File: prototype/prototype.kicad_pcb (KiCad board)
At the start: 4 copper layers, 78.7 x 63.5 mm, 47 parts, among them P1 CONN_25X2, P2 CONN_25X2, P3 VGACONN, U1 MC68SEC000, U2 FLASHROM_512K_16, U3 RAM_512K_16, U4 RAM_512K_16

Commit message: Reassign mojo header pins to move VGA to the other end.
There is no room at the left-hand edge for the VGA connector because the
AVR header is in the way, so we need to move it to the right-hand edge.
To ease routing, the signals should therefore be exposed at that end too.
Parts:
- moved D10 360.0 mm to (55.5, 48.9)
- moved D5 360.0 mm to (39.0, 48.9)
- moved D6 360.0 mm to (45.5, 48.9)
- moved D7 360.0 mm to (52.0, 48.9)
- moved D8 360.0 mm to (42.5, 48.9)
- moved D9 360.0 mm to (49.0, 48.9)
- moved P3 360.0 mm to (48.0, 34.9)
- moved R11 360.0 mm to (58.6, 57.0)
- moved R13 360.0 mm to (54.8, 57.0)
- moved R14 360.0 mm to (69.4, 40.5)
- moved R15 360.0 mm to (69.4, 42.4)
- moved R2 360.0 mm to (38.9, 57.0)
- moved R4 360.0 mm to (42.7, 57.0)
- moved R7 360.0 mm to (49.7, 57.0)
- moved R9 360.0 mm to (45.9, 57.0)
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
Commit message: Assign appropriate footprints to the memory ICs.
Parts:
- D1, D10, D2, D3, D4, D5, D6, D7, D8, D9: footprint Diodes_SMD:Diode_SOT23_Handsoldering -> 68k-computer:SOT-23_Diode
- U2: footprint SSOP_Packages:TSSOP-48_6.1x12.5mm_Pitch0.5mm -> 68k-computer:TSOP-48
- U3, U4: footprint SMD_Packages:PLCC-44 -> 68k-computer:TSOP-44
- moved U2 324.6 mm to (134.6, 101.6), turned to 270 degrees
- moved U4 252.1 mm to (158.1, 80.0), turned to 90 degrees
- moved D1 218.5 mm to (229.7, 41.3)
- moved D2 218.5 mm to (229.2, 25.3)
- moved D3 218.5 mm to (239.2, 33.3)
- moved D4 218.5 mm to (228.7, 33.8)
- moved U3 200.5 mm to (134.6, 80.0), turned to 90 degrees
- moved P3 187.9 mm to (188.5, 159.7), turned to 0 degrees
- moved D5 185.7 mm to (197.5, 145.7), turned to 180 degrees
- moved R3 181.5 mm to (199.6, 137.6), turned to 90 degrees
- moved D8 179.7 mm to (194.0, 145.7), turned to 180 degrees
- moved R2 178.0 mm to (197.7, 137.6), turned to 90 degrees
- moved D6 174.7 mm to (191.0, 145.7), turned to 180 degrees
- moved R5 174.7 mm to (195.8, 137.6), turned to 90 degrees
- moved R4 171.3 mm to (193.8, 137.6), turned to 90 degrees
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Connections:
- P1 pad 10: RED3 -> A1
- P1 pad 11: GREEN0 -> A2
- P1 pad 12: GREEN1 -> A3
- P1 pad 13: GREEN2 -> A4
- P1 pad 14: GREEN3 -> A5
- P1 pad 15: ~BERR -> A6
- P1 pad 16: ~IPL2 -> A7
- P1 pad 17: ~IPL1 -> A8
- P1 pad 18: ~IPL0 -> A9
- P1 pad 19: FC2 -> A10
- P1 pad 20: FC1 -> A11
- P1 pad 21: FC0 -> LA12
- P1 pad 22: A1 -> LA13
- P1 pad 23: A2 -> LA14
- P1 pad 24: A3 -> LA15
- P1 pad 25: A4 -> LA16
- P1 pad 26: A5 -> LA17
- P1 pad 27: A6 -> LA18
- P1 pad 28: A7 -> LA19
- P1 pad 29: A8 -> LA20
- P1 pad 30: A9 -> LA21
- P1 pad 31: A10 -> LA22
- P1 pad 32: A11 -> LA23
- P1 pad 33: LA12 -> RED0
- P1 pad 34: LA13 -> RED1
- P1 pad 35: LA14 -> RED2
- P1 pad 36: LA15 -> RED3
- P1 pad 37: LA16 -> GREEN0
- P1 pad 38: LA17 -> GREEN1
- P1 pad 39: LA18 -> GREEN2
- P1 pad 40: LA19 -> GREEN3
- P1 pad 41: LA20 -> BLUE0
- P1 pad 42: LA21 -> BLUE1
- P1 pad 43: LA22 -> BLUE2
- P1 pad 44: LA23 -> BLUE3
- P1 pad 7: RED0 -> FC2
- P1 pad 8: RED1 -> FC1
- P1 pad 9: RED2 -> FC0
- P2 pad 10: BLUE3 -> PA17
- P2 pad 11: PA12 -> PA18
- P2 pad 12: PA13 -> PA19
- P2 pad 13: PA14 -> ~RE
- P2 pad 14: PA15 -> ~WE
- P2 pad 15: PA16 -> ~IPL0
- P2 pad 16: PA17 -> ~IPL1
- P2 pad 17: PA18 -> ~IPL2
- P2 pad 18: PA19 -> ~BERR
- P2 pad 19: ~RE -> CLK
- P2 pad 20: ~WE -> ~DTACK
- P2 pad 21: CLK -> R/~W
- P2 pad 22: ~DTACK -> ~LDS
- P2 pad 23: R/~W -> ~UDS
- P2 pad 24: ~LDS -> ~AS
- P2 pad 25: ~UDS -> D0
- P2 pad 26: ~AS -> D1
- P2 pad 27: D0 -> D2
- P2 pad 28: D1 -> D3
- P2 pad 29: D2 -> D4
- P2 pad 30: D3 -> D5
- P2 pad 31: D4 -> D6
- P2 pad 32: D5 -> D7
- P2 pad 33: D6 -> D8
- P2 pad 34: D7 -> D9
- P2 pad 35: D8 -> D10
- P2 pad 36: D9 -> D11
- P2 pad 37: D10 -> D12
- P2 pad 38: D11 -> D13
- P2 pad 39: D12 -> D14
- P2 pad 40: D13 -> D15
- P2 pad 41: D14 -> HSYNC
- P2 pad 42: D15 -> VSYNC
- P2 pad 5: HSYNC -> PA12
- P2 pad 6: VSYNC -> PA13
- P2 pad 7: BLUE0 -> PA14
- P2 pad 8: BLUE1 -> PA15
- P2 pad 9: BLUE2 -> PA16

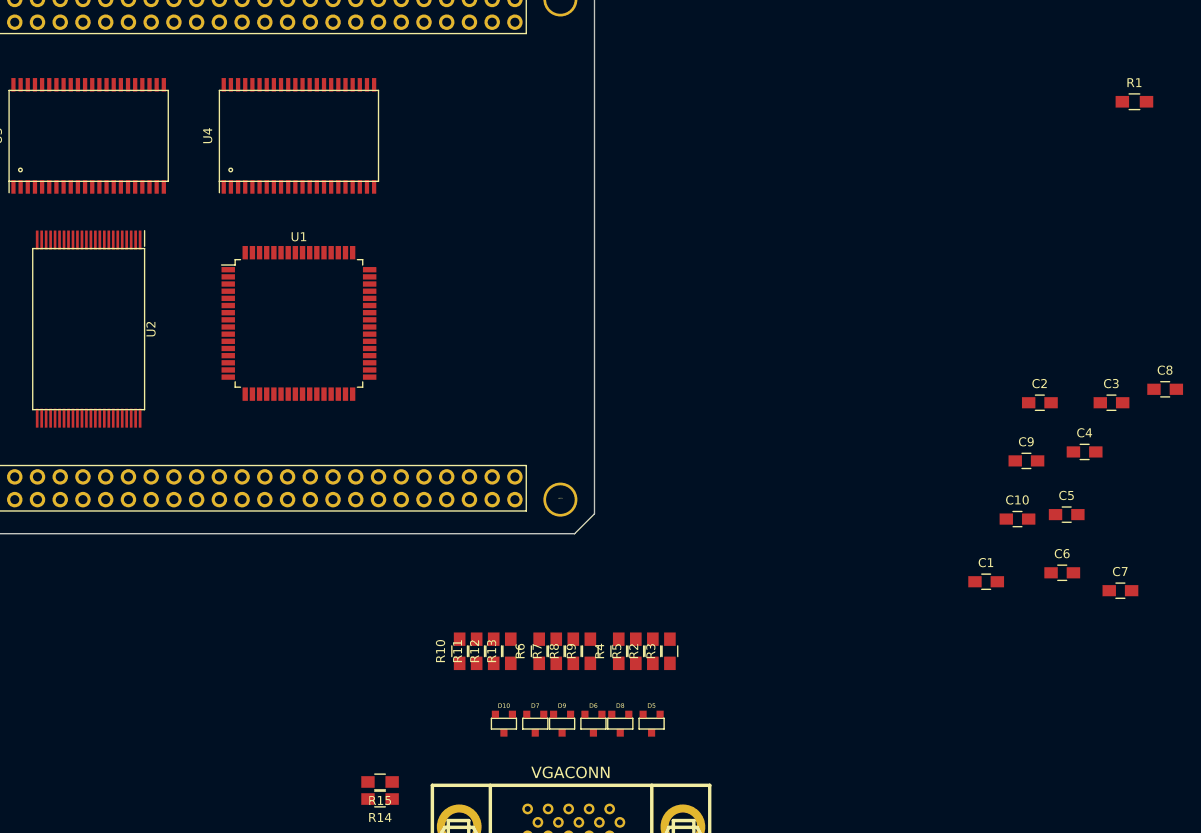
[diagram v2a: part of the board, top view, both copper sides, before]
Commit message: Configure the design rules to match OSH Park 4-layer.
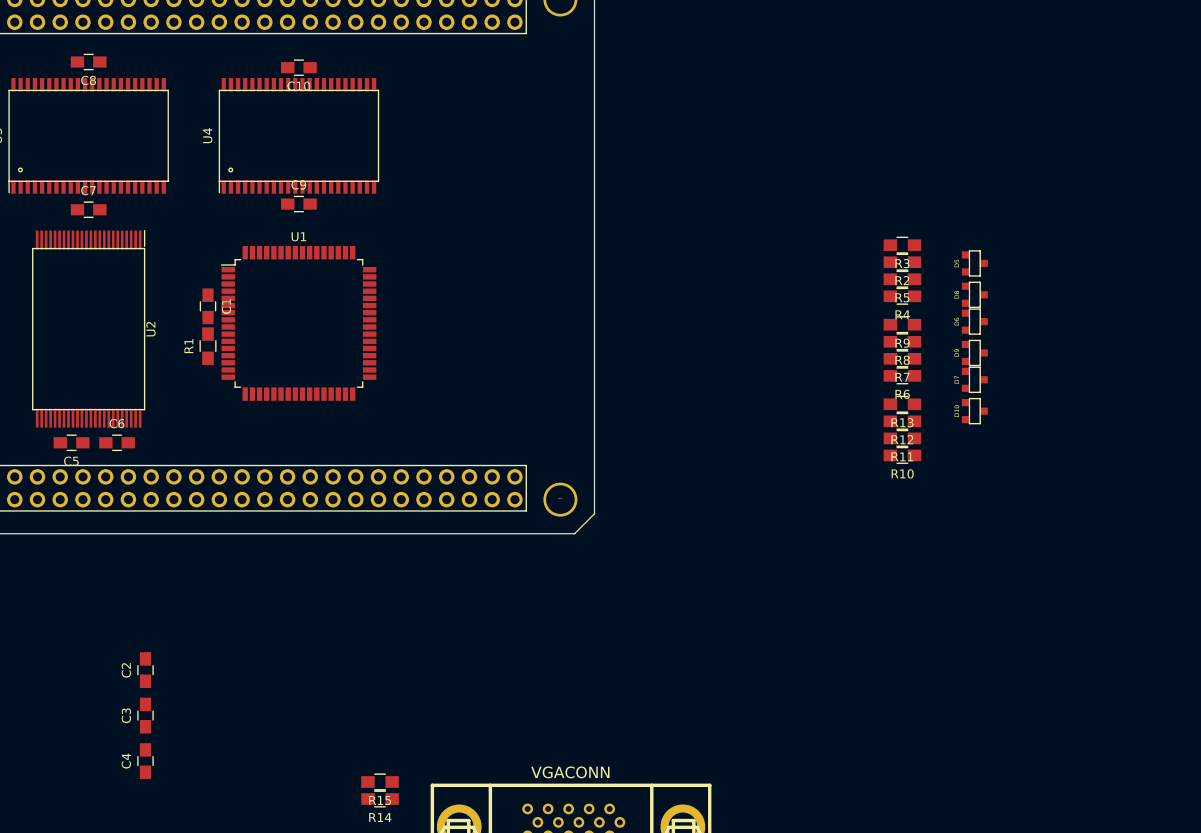
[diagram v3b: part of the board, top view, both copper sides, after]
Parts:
- moved C8 125.7 mm to (134.6, 71.8), turned to 180 degrees
- moved C7 122.9 mm to (134.6, 88.3)
- moved C3 113.4 mm to (141.0, 144.8), turned to 90 degrees
- moved C5 111.5 mm to (132.7, 114.3), turned to 180 degrees
- moved C4 110.5 mm to (141.0, 149.9), turned to 90 degrees
- moved R1 107.0 mm to (148.0, 103.5), turned to 90 degrees
- moved C6 106.6 mm to (137.8, 114.3)
- moved C2 104.3 mm to (141.0, 139.7), turned to 90 degrees
- moved C10 94.8 mm to (158.1, 72.4), turned to 180 degrees
- moved C1 92.2 mm to (148.0, 99.1), turned to 270 degrees
- moved C9 86.2 mm to (158.1, 87.6)
- moved D10 63.1 mm to (233.6, 110.8), turned to 270 degrees
- moved D5 62.8 mm to (233.6, 94.3), turned to 270 degrees
- moved D7 62.4 mm to (233.6, 107.3), turned to 270 degrees
- moved D8 62.2 mm to (233.6, 97.8), turned to 270 degrees
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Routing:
- removed copper zone on GND.Cu, net GND
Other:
- net class Default: clearance 0.1 -> 0.127; trace_width 0.1 -> 0.2032; via_dia 0.889 -> 0.3556; via_drill 0.635 -> 0.254
- net class Power: clearance 0.3 -> 0.127; trace_width 0.3 -> 0.508; via_dia 0.889 -> 0.6096; via_drill 0.635 -> 0.254
- rule trace_clearance: 0.1 -> 0.127
- rule trace_min: 0.1 -> 0.127
- rule via_min_drill: 0.508 -> 0.254
- rule via_min_size: 0.889 -> 0.3

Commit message: Add copper fills to the GND and VCC layers.
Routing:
- added copper zone on GND.Cu, net GND
- added copper zone on VCC.Cu, net VCC
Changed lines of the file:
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@@
   (general
     (links 268)
-    (no_connects 268)
+    (no_connects 264)
     (area 112.344999 23.59 257.520001 167.285001)
     (thickness 1.6)
@@
   (layers
     (0 F.Cu signal)
-    (1 GND.Cu power)
-    (2 VCC.Cu power)
+    (1 GND.Cu power hide)
+    (2 VCC.Cu power hide)
     (31 B.Cu signal)
     (32 B.Adhes user)
@@
   (gr_line (start 191.135 122.2375) (end 188.9125 124.46) (angle 90) (layer Edge.Cuts) (width 0.1))
   (gr_line (start 112.395 63.1825) (end 114.6175 60.96) (angle 90) (layer Edge.Cuts) (width 0.1))
+  (zone (net 2) (net_name GND) (layer GND.Cu) (hatch edge 0.508)
+    (connect_pads (clearance 0.508))
+    (min_thickness 0.254)
+    (fill yes (arc_segments 16) (thermal_gap 0.508) (thermal_bridge_width 0.508))
+    (polygon
+      (pts
+        (xy 190.373 121.666) (xy 188.341 123.698) (xy 115.189 123.698) (xy 113.157 121.666) (xy 113.157 63.754)
+        (xy 115.189 61.722) (xy 188.341 61.722) (xy 190.373 63.754)
+      )
+    )
+  )
+  (zone (net 1) (net_name VCC) (layer VCC.Cu) (hatch edge 0.508)
+    (connect_pads (clearance 0.508))
+    (min_thickness 0.254)
+    (fill yes (arc_segments 16) (thermal_gap 0.508) (thermal_bridge_width 0.508))
+    (polygon
+      (pts
+        (xy 190.373 121.666) (xy 188.341 123.698) (xy 115.189 123.698) (xy 113.157 121.666) (xy 113.157 63.754)
+        (xy 115.189 61.722) (xy 188.341 61.722) (xy 190.373 63.754)
+      )
+    )
+  )
 )

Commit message: PCB floor planning.
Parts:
- moved R14 82.5 mm to (172.0, 71.7), turned to 90 degrees
- moved R15 80.8 mm to (174.3, 71.7), turned to 90 degrees
- moved D2 75.5 mm to (169.0, 71.0), turned to 90 degrees
- moved D3 74.0 mm to (177.3, 74.0), turned to 90 degrees
- moved P3 73.8 mm to (185.3, 86.0), turned to 270 degrees
- moved D1 68.9 mm to (169.0, 74.0), turned to 90 degrees
- moved R3 67.0 mm to (162.0, 113.5), turned to 270 degrees
- moved R2 64.5 mm to (164.0, 113.5), turned to 270 degrees
- moved D4 63.4 mm to (177.3, 71.0), turned to 90 degrees
- moved R5 62.0 mm to (166.0, 113.5), turned to 270 degrees
- moved C4 61.8 mm to (159.8, 91.0), turned to 180 degrees
- moved R4 59.6 mm to (168.0, 113.5), turned to 270 degrees
- moved D5 58.2 mm to (177.0, 107.7), turned to 90 degrees
- moved D8 57.0 mm to (177.0, 104.5), turned to 90 degrees
- moved R7 54.9 mm to (171.3, 113.5), turned to 270 degrees
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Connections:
- D1 pad 1: VCC -> HSYNC
- D1 pad 2: Net-(D1-Pad2) -> VCC
- D2 pad 2: Net-(D1-Pad2) -> HSYNC
- D3 pad 1: VCC -> VSYNC
- D3 pad 2: Net-(D3-Pad2) -> VCC
- D4 pad 2: Net-(D3-Pad2) -> VSYNC

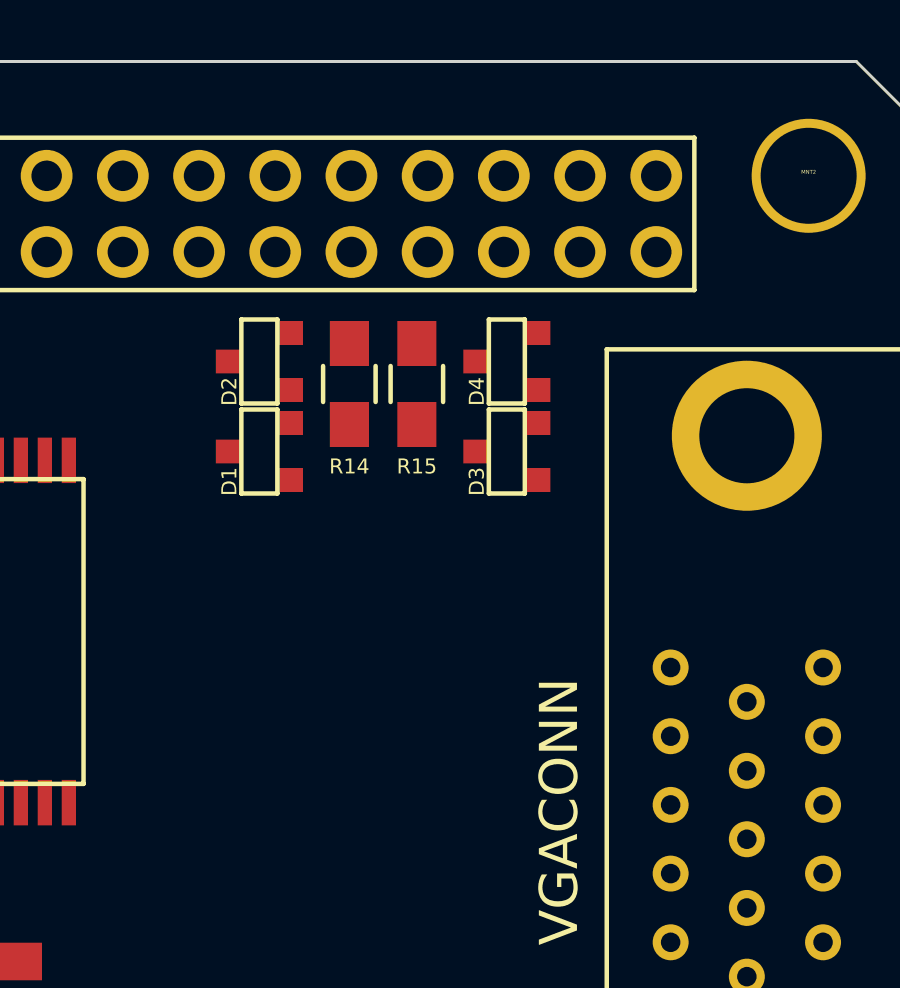
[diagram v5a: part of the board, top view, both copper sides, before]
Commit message: Route the HSYNC and VSYNC signals.
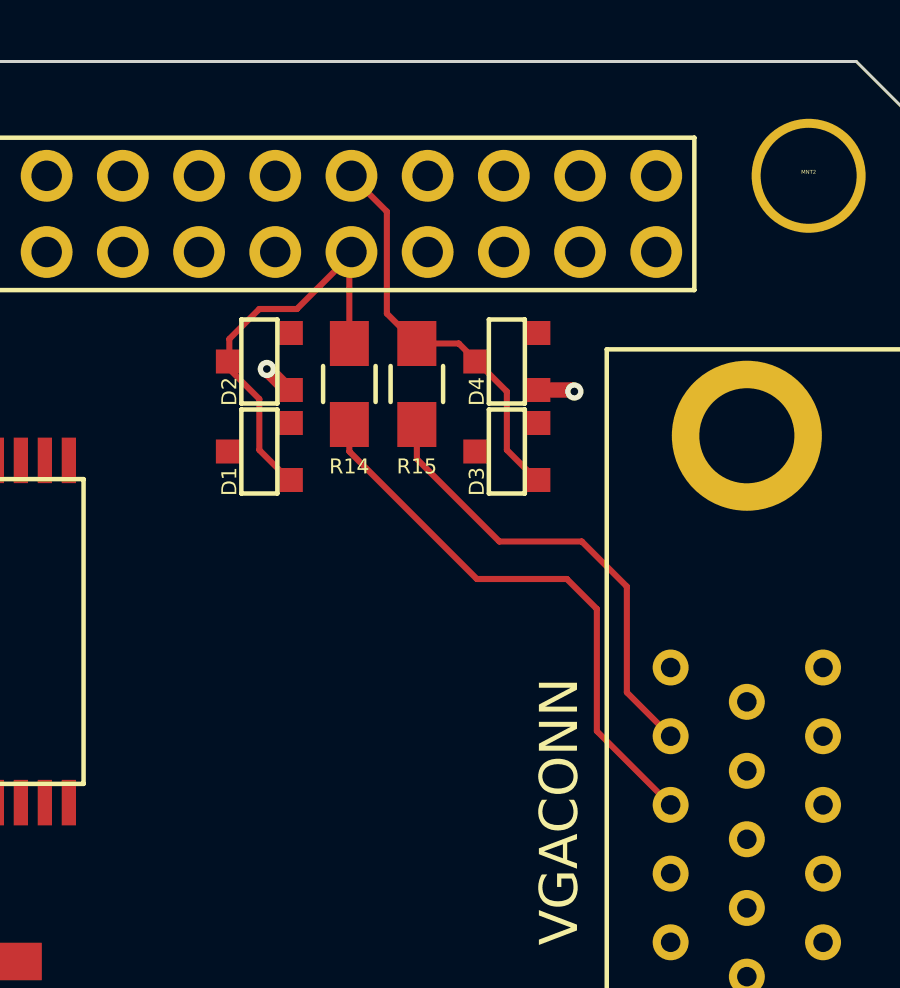
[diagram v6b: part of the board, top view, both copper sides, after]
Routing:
- net Net-(P3-Pad13): track 0.00 -> 18.9 mm
- net Net-(P3-Pad14): track 0.00 -> 15.5 mm
- net HSYNC: track 0.00 -> 14.1 mm
- net VSYNC: track 0.00 -> 13.5 mm
- net GND: track 0.00 -> 2.31 mm, vias 0 -> 2
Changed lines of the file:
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@@
   (general
     (links 270)
-    (no_connects 261)
+    (no_connects 252)
     (area 112.344999 60.909999 191.185001 124.510001)
     (thickness 1.6)
     (drawings 9)
-    (tracks 0)
+    (tracks 38)
     (zones 0)
     (modules 47)
@@
   (gr_line (start 191.135 122.2375) (end 188.9125 124.46) (angle 90) (layer Edge.Cuts) (width 0.1))
   (gr_line (start 112.395 63.1825) (end 114.6175 60.96) (angle 90) (layer Edge.Cuts) (width 0.1))
+  (segment (start 170.015 71.91) (end 169.965 71.91) (width 0.508) (layer F.Cu) (net 2) (status C00000))
+  (segment (start 169.965 71.91) (end 169.265 71.21) (width 0.508) (layer F.Cu) (net 2) (status 400000))
+  (via (at 169.265 71.21) (size 0.6096) (layers F.Cu B.Cu) (net 2))
+  (segment (start 178.265 71.91) (end 179.465 71.91) (width 0.508) (layer F.Cu) (net 2) (status 400000))
+  (via (at 179.515 71.96) (size 0.6096) (layers F.Cu B.Cu) (net 2))
+  (segment (start 179.465 71.91) (end 179.515 71.96) (width 0.508) (layer F.Cu) (net 2))
+  (segment (start 172.085 67.31) (end 172.085 67.39) (width 0.2032) (layer F.Cu) (net 44) (status C00000))
+  (segment (start 172.085 67.39) (end 170.265 69.21) (width 0.2032) (layer F.Cu) (net 44) (status 400000))
+  (segment (start 168.015 70.21) (end 168.015 70.96) (width 0.2032) (layer F.Cu) (net 44) (status 800000))
+  (segment (start 169.015 69.21) (end 168.015 70.21) (width 0.2032) (layer F.Cu) (net 44))
+  (segment (start 170.265 69.21) (end 169.015 69.21) (width 0.2032) (layer F.Cu) (net 44))
+  (segment (start 172.015 70.36) (end 172.015 67.38) (width 0.2032) (layer F.Cu) (net 44) (status C00000))
+  (segment (start 172.015 67.38) (end 172.085 67.31) (width 0.2032) (layer F.Cu) (net 44) (status C00000))
+  (segment (start 168.015 70.96) (end 168.015 71.21) (width 0.2032) (layer F.Cu) (net 44) (status C00000))
+  (segment (start 168.015 71.21) (end 169.015 72.21) (width 0.2032) (layer F.Cu) (net 44) (status 400000))
+  (segment (start 169.015 73.91) (end 170.015 74.91) (width 0.2032) (layer F.Cu) (net 44) (status 800000))
+  (segment (start 169.015 72.21) (end 169.015 73.91) (width 0.2032) (layer F.Cu) (net 44))
+  (segment (start 172.015 70.36) (end 171.865 70.36) (width 0.2032) (layer F.Cu) (net 44) (status C00000))
+  (segment (start 172.085 64.77) (end 172.085 64.78) (width 0.2032) (layer F.Cu) (net 45) (status C00000))
+  (segment (start 172.085 64.78) (end 173.265 65.96) (width 0.2032) (layer F.Cu) (net 45) (status 400000))
+  (segment (start 173.265 65.96) (end 173.265 69.36) (width 0.2032) (layer F.Cu) (net 45))
+  (segment (start 173.265 69.36) (end 174.265 70.36) (width 0.2032) (layer F.Cu) (net 45) (status 800000))
+  (segment (start 174.265 70.36) (end 175.665 70.36) (width 0.2032) (layer F.Cu) (net 45) (status 400000))
+  (segment (start 177.265 73.91) (end 178.265 74.91) (width 0.2032) (layer F.Cu) (net 45) (status 800000))
+  (segment (start 177.265 71.96) (end 177.265 73.91) (width 0.2032) (layer F.Cu) (net 45))
+  (segment (start 175.665 70.36) (end 177.265 71.96) (width 0.2032) (layer F.Cu) (net 45))
+  (segment (start 172.015 73.06) (end 172.015 73.96) (width 0.2032) (layer F.Cu) (net 91) (status 400000))
+  (segment (start 180.265 83.28) (end 182.725 85.74) (width 0.2032) (layer F.Cu) (net 91) (status 800000))
+  (segment (start 180.265 79.21) (end 180.265 83.28) (width 0.2032) (layer F.Cu) (net 91))
+  (segment (start 179.265 78.21) (end 180.265 79.21) (width 0.2032) (layer F.Cu) (net 91))
+  (segment (start 176.265 78.21) (end 179.265 78.21) (width 0.2032) (layer F.Cu) (net 91))
+  (segment (start 172.015 73.96) (end 176.265 78.21) (width 0.2032) (layer F.Cu) (net 91))
+  (segment (start 174.265 73.06) (end 174.265 74.21) (width 0.2032) (layer F.Cu) (net 92) (status 400000))
+  (segment (start 181.265 81.99) (end 182.725 83.45) (width 0.2032) (layer F.Cu) (net 92) (status 800000))
+  (segment (start 181.265 78.46) (end 181.265 81.99) (width 0.2032) (layer F.Cu) (net 92))
+  (segment (start 179.765 76.96) (end 181.265 78.46) (width 0.2032) (layer F.Cu) (net 92))
+  (segment (start 177.015 76.96) (end 179.765 76.96) (width 0.2032) (layer F.Cu) (net 92))
+  (segment (start 174.265 74.21) (end 177.015 76.96) (width 0.2032) (layer F.Cu) (net 92))
   (zone (net 2) (net_name GND) (layer GND.Cu) (hatch edge 0.508)
     (connect_pads (clearance 0.508))
